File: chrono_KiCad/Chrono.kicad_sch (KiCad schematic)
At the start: 16 parts, among them SW1 SW_Push, U1 ATtiny85-20P, U2 LM393, U3 ER_OLEDM0.91_1x-I2C

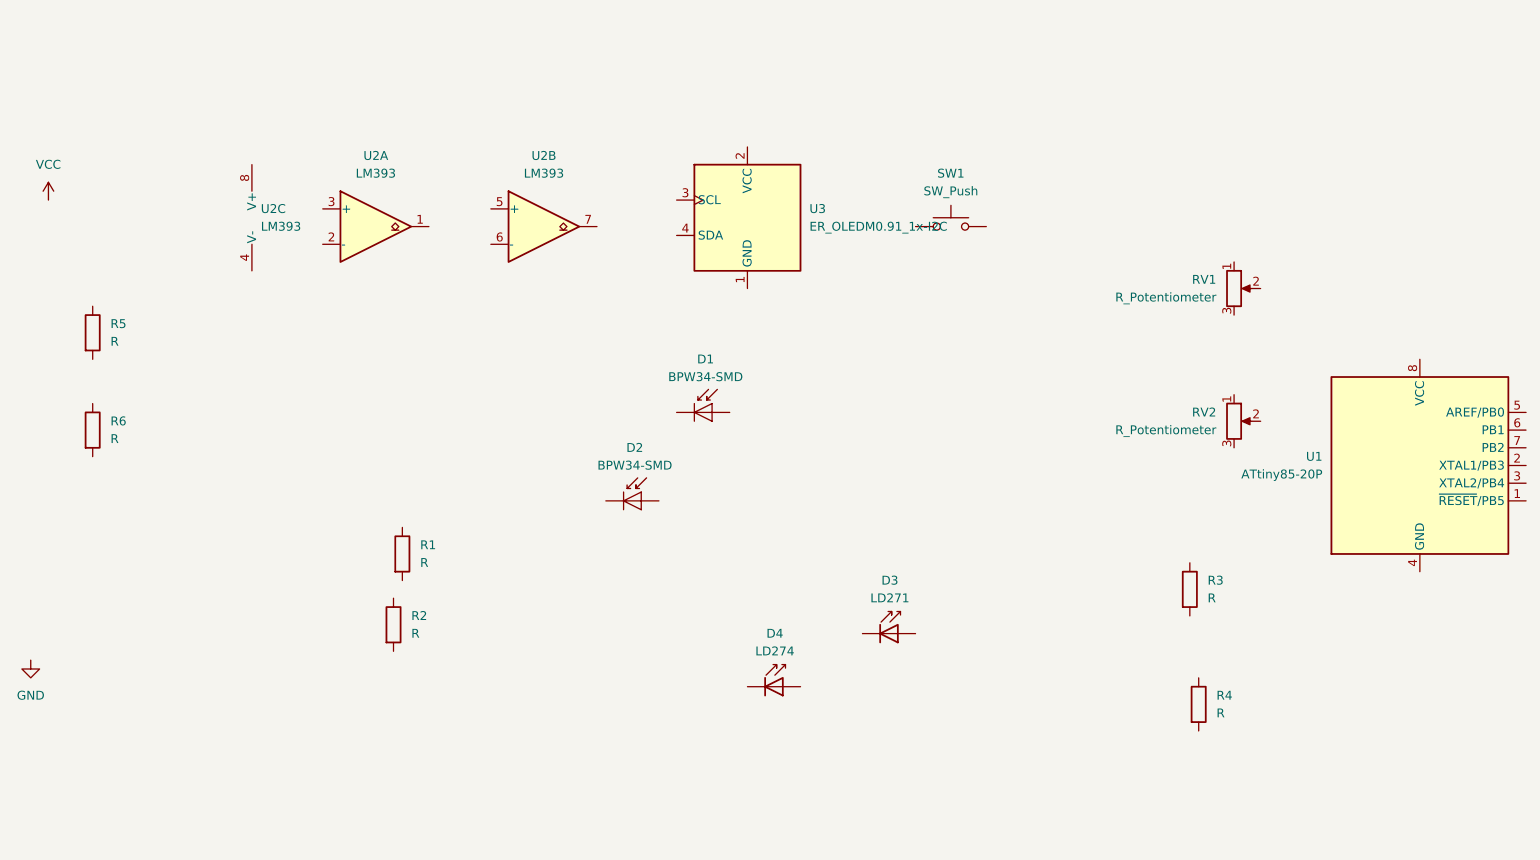
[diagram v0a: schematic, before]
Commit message: KiCad schematic finished and exported to pdf
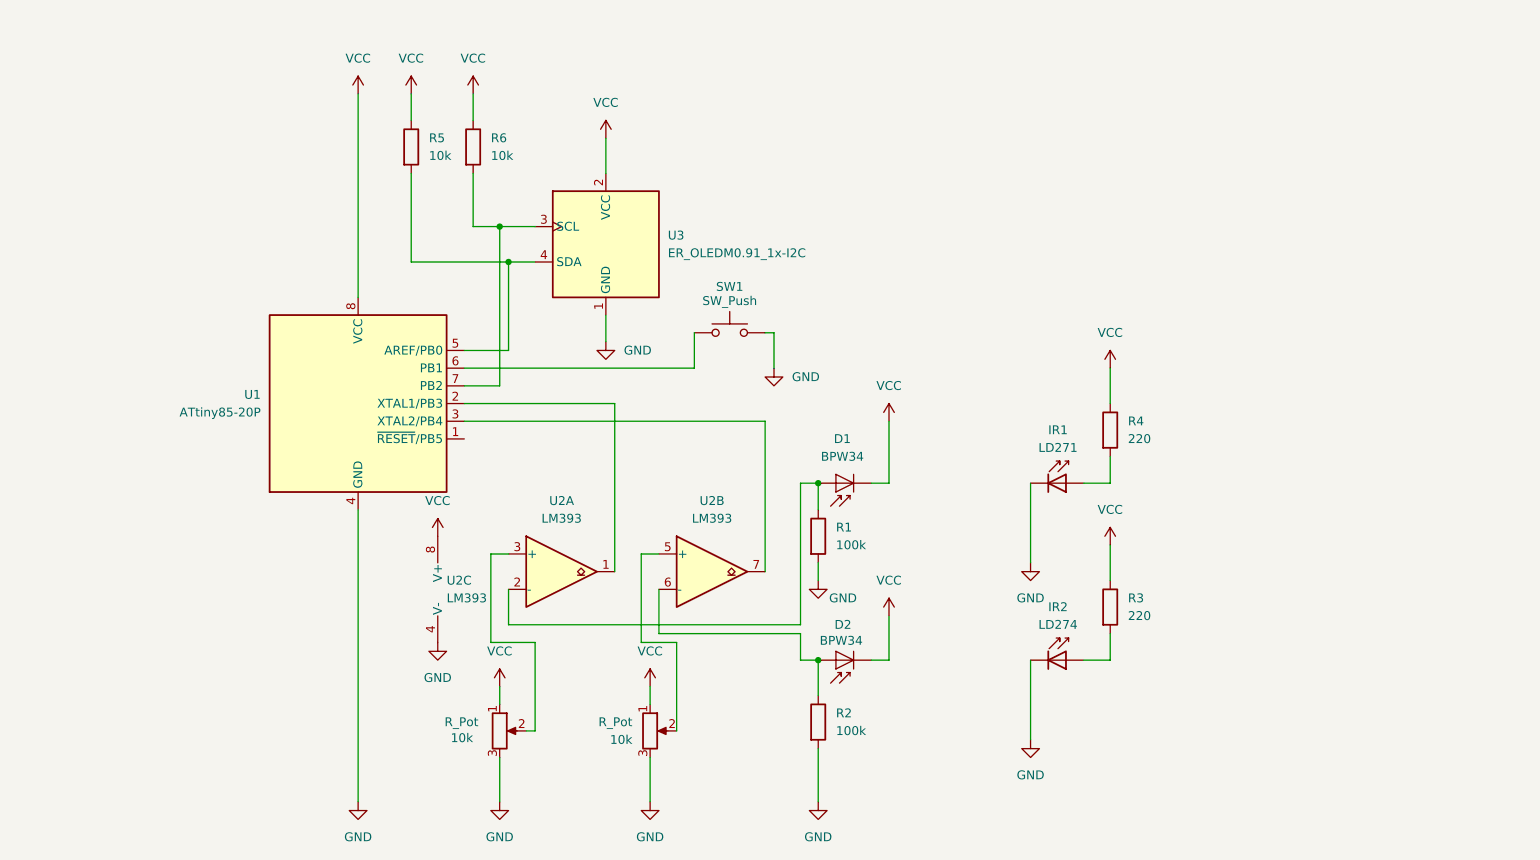
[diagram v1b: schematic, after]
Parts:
- D1, D2: value BPW34-SMD -> BPW34
- R1, R2: value R -> 100k
- R3, R4: value R -> 220
- R5, R6: value R -> 10k
- R_Pot: renamed from RV1; value R_Potentiometer -> 10k
- R_Pot: renamed from RV2; value R_Potentiometer -> 10k
- renumbered D3 to IR1, D4 to IR2
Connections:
- net GND: now also IR1.1 (K), IR2.1 (K), R1.2, R2.2, R_Pot.3, R_Pot.3, SW1.2, U1.4 (GND), U2.4 (V-), U3.1 (GND)
- net VCC: now also D1.1 (K), D2.1 (K), R3.1, R4.1, R5.1, R6.1, R_Pot.1, R_Pot.1, U1.8 (VCC), U2.8 (V+), U3.2 (VCC)
- net at R4.2: now also IR1.2 (A)
- net at SW1.1: now also U1.6 (PB1)
- net at U2.5 (+): now also R_Pot.2
- net at U2.6 (-): now also D2.2 (A), R2.1
- net at U2.7: now also U1.3 (XTAL2/PB4)
- net at D1.2 (A): now also R1.1, U2.2 (-)
- net at U1.2 (XTAL1/PB3): now also U2.1
- net at U1.5 (AREF/PB0): now also R5.2, U3.4 (SDA)
- net at U1.7 (PB2): now also R6.2, U3.3 (SCL)
- net at R_Pot.2: now also U2.3 (+)
- net at R3.2: now also IR2.2 (A)
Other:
- moved on the sheet: D1, D2, IR1, IR2, R1, R2, R3, R4, R5, R6, R_Pot, SW1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

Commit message: Switching gate1 and gate 2
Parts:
- added R7, R8: 10k, symbol Device:R
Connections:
- net VCC: now also R7.1, R8.1
- net at U1.3 (XTAL2/PB4), U2.7: now also R8.2
- net at U1.2 (XTAL1/PB3), U2.1: now also R7.2
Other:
- moved on the sheet: R5, R6, SW1, U3
